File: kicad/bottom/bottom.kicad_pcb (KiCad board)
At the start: 2 copper layers, 62 x 119.5 mm, 17 parts, among them J1 Conn_01x15_Socket

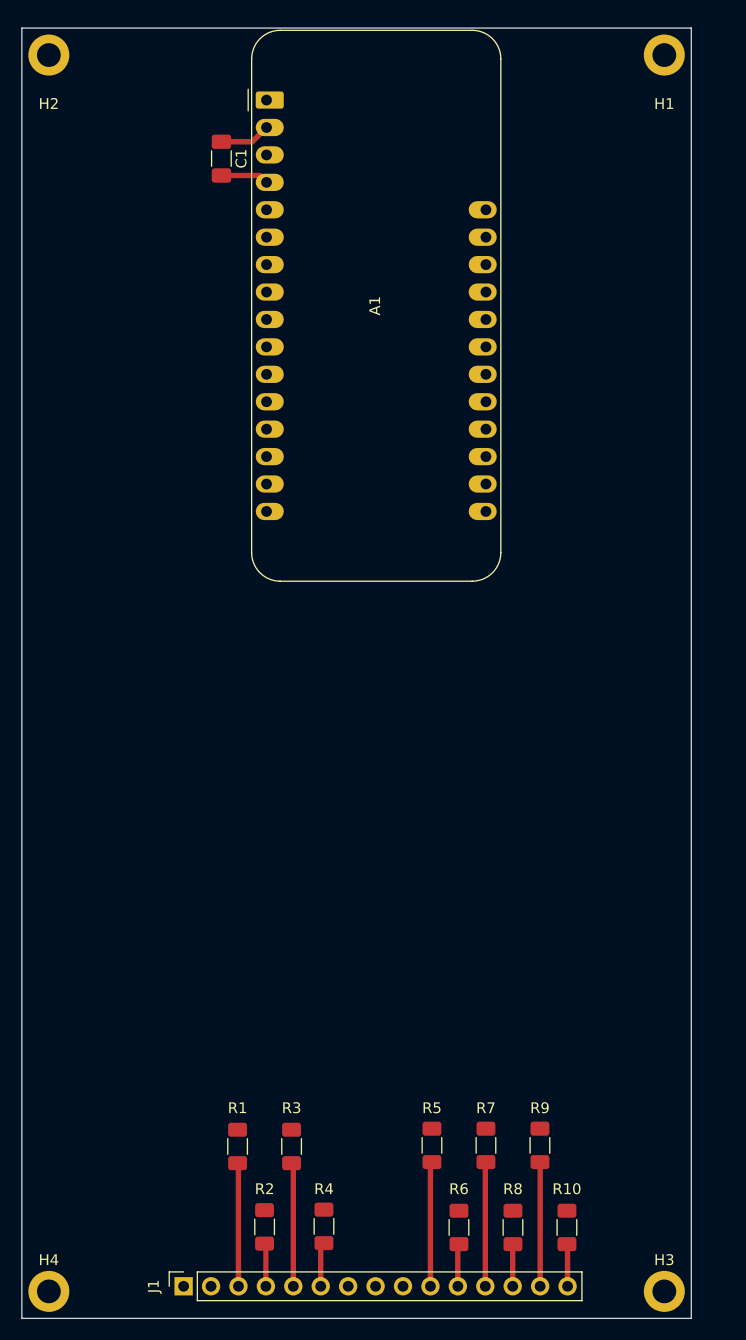
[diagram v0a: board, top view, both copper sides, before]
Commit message: delete duplicate top folder, finished wiring on bottom pcb, need better wiring on top pcb
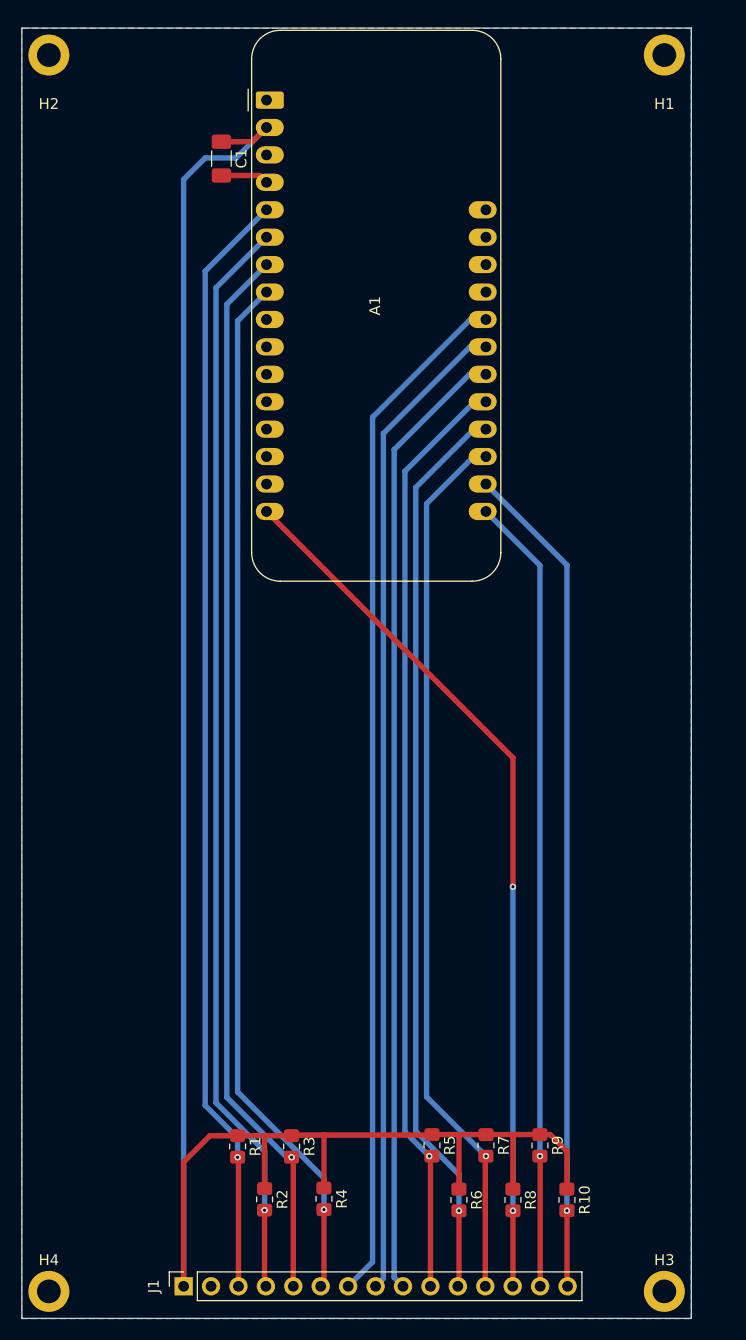
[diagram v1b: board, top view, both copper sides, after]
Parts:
- R1, R10, R2, R3, R4, R5, R6, R7, R8, R9: footprint Resistor_SMD:R_1206_3216Metric_Pad1.30x1.75mm_HandSolder -> Resistor_SMD:R_0805_2012Metric_Pad1.20x1.40mm_HandSolder
- moved R10 2.55 mm to (66.0, 125.0)
- moved R2 2.55 mm to (38.0, 125.0)
- moved R4 2.55 mm to (43.5, 124.9)
- moved R6 2.55 mm to (56.0, 125.0)
- moved R8 2.55 mm to (61.0, 125.0)
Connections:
- H1 pad 1: unconnected-(H1-Pad1) -> GND
- H2 pad 1: unconnected-(H2-Pad1) -> GND
- H3 pad 1: unconnected-(H3-Pad1) -> GND
- H4 pad 1: unconnected-(H4-Pad1) -> GND
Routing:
- net +3.3V: track 4.73 -> 188.9 mm
- net BT_SELECT: track 3.83 -> 100.8 mm, vias 0 -> 1
- net COL0: track 0.00 -> 95.7 mm
- net ENC_CLK: track 3.70 -> 96.2 mm, vias 0 -> 1
- net COL1: track 0.00 -> 92.1 mm
- net ENC_DT: track 11.3 -> 102.7 mm, vias 0 -> 1
- net COL2: track 0.00 -> 89.2 mm
- net ENC_SW: track 11.2 -> 98.2 mm, vias 0 -> 1
- net ROW2: track 3.80 -> 83.2 mm, vias 0 -> 1
- net ROW0: track 3.88 -> 81.2 mm, vias 0 -> 2
- net OLED_SCL: track 3.84 -> 77.3 mm, vias 0 -> 1
- net ROW3: track 11.4 -> 84.8 mm, vias 0 -> 1
- net ROW1: track 11.4 -> 80.3 mm, vias 0 -> 1
- net OLED_SDA: track 11.5 -> 73.3 mm, vias 0 -> 1
- added copper zone on B.Cu, net GND

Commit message: on bottom pcb moved signal connections from back copper to front, left most back copper as ground plane. aligned pins and pin sockets on top and bottom pcb, centered them.
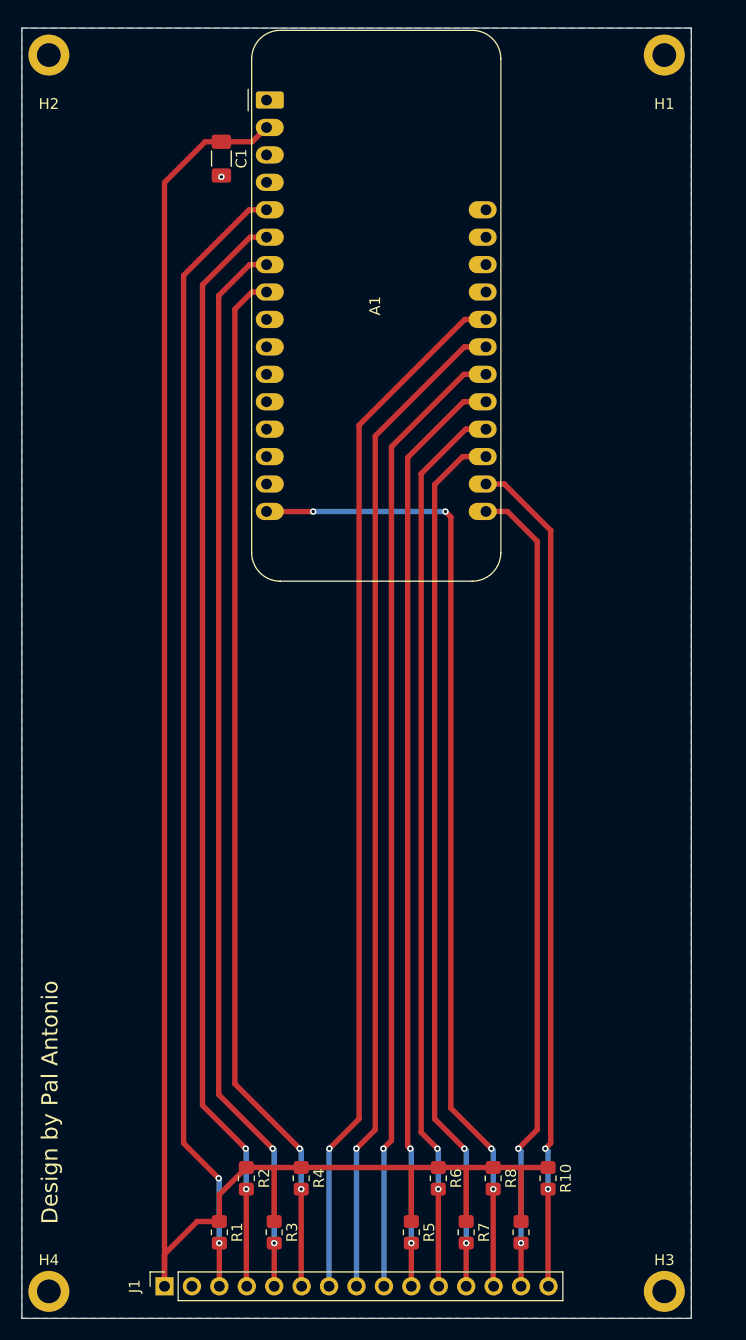
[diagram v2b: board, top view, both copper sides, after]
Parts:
- moved R5 8.27 mm to (51.6, 128.0)
- moved R7 8.26 mm to (56.7, 128.0)
- moved R9 8.24 mm to (61.8, 128.0)
- moved R1 8.13 mm to (33.8, 128.0)
- moved R3 8.11 mm to (38.9, 128.0)
- moved R4 2.84 mm to (41.4, 123.0)
- moved R6 2.77 mm to (54.1, 123.0)
- moved R8 2.71 mm to (59.2, 123.0)
- moved R10 2.66 mm to (64.2, 123.0)
- moved R2 2.58 mm to (36.3, 123.0)
- moved J1 1.77 mm to (28.7, 133.0)
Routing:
- net +3.3V: track 188.9 -> 177.2 mm
- net ROW0: track 81.2 -> 90.2 mm, vias 2 -> 4
- net GND: track 4.44 -> 0.00 mm, vias 0 -> 1
- net ENC_DT: track 102.7 -> 105.2 mm, vias 1 -> 2
- net OLED_SDA: track 73.3 -> 75.7 mm, vias 1 -> 2
- net ROW3: track 84.8 -> 86.3 mm, vias 1 -> 2
- net BT_SELECT: track 100.8 -> 102.2 mm, vias 1 -> 2
- net ENC_SW: track 98.2 -> 99.5 mm, vias 1 -> 2
- net COL1: track 92.1 -> 93.1 mm, vias 0 -> 1
- net COL0: track 95.7 -> 96.7 mm, vias 0 -> 1
- net ROW1: track 80.3 -> 81.3 mm, vias 1 -> 2
- net OLED_SCL: track 77.3 -> 78.1 mm, vias 1 -> 2
- net ROW2: track 83.2 -> 83.6 mm, vias 1 -> 2
- net ENC_CLK: track 96.2 -> 96.6 mm, vias 1 -> 2
- net COL2: track 89.2 -> 89.6 mm, vias 0 -> 1
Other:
- board text added: "Design by Pal Antonio"

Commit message: added cutout for battery jst connector on bottom pcb
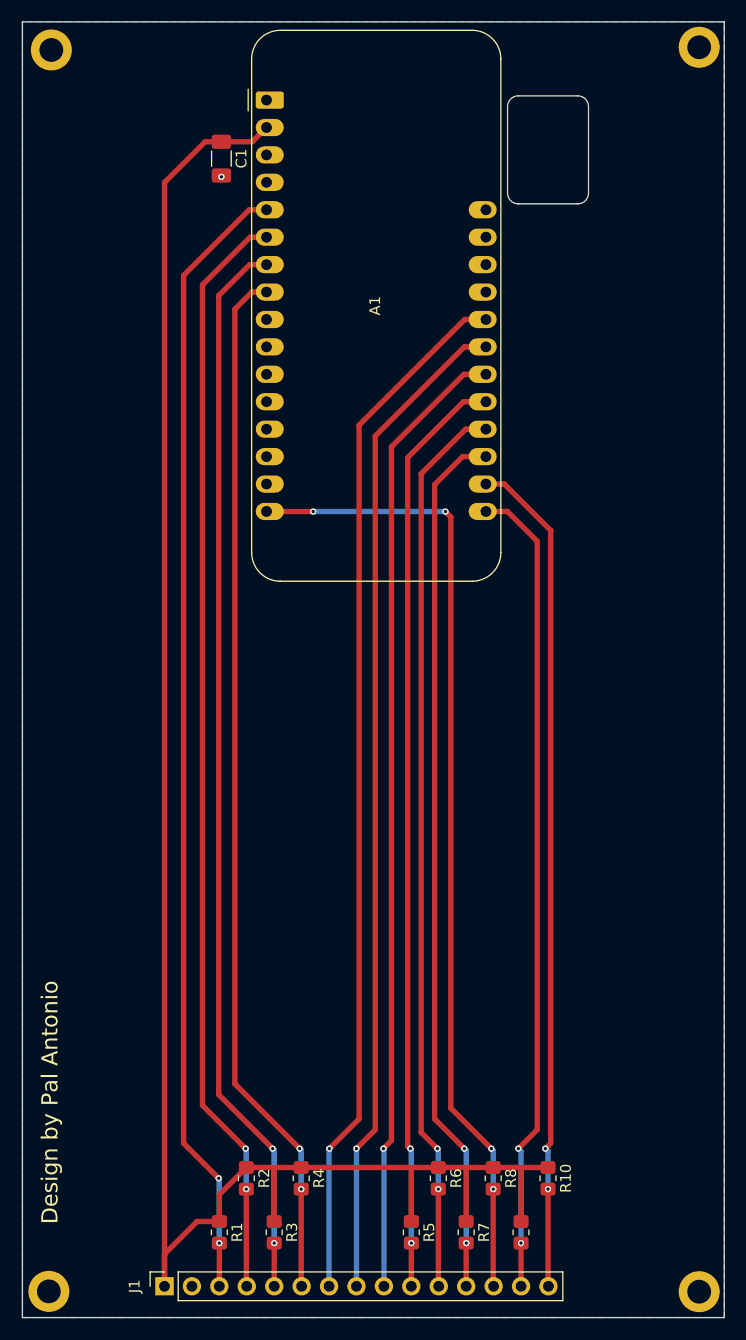
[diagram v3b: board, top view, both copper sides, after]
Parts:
- moved H2 60.2 mm to (78.2, 18.2)
- moved H1 56.8 mm to (18.2, 18.5)
- moved H3 3.23 mm to (78.2, 133.5)
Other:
- board size 62 x 119.5 mm -> 65 x 120 mm

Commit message: moved pull up res closer to pins on bottom pcb
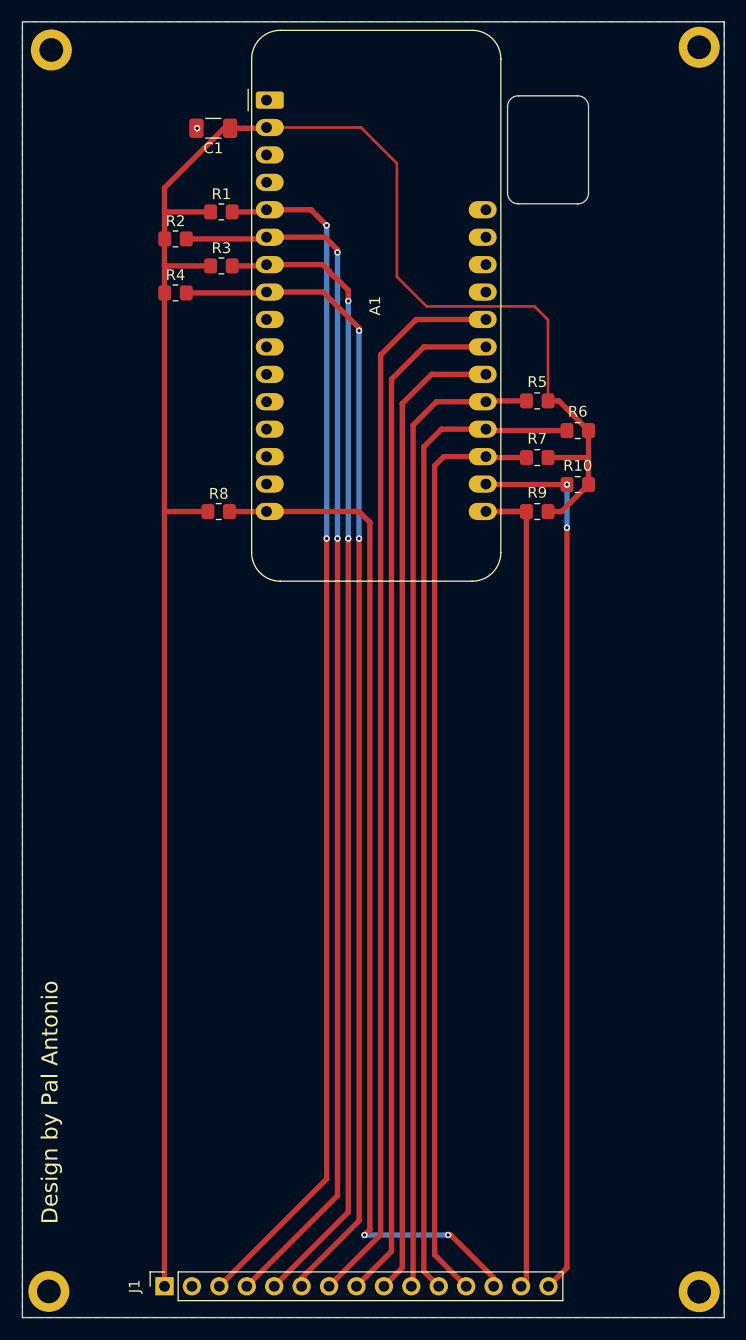
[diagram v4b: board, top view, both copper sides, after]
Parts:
- moved R1 94.5 mm to (34.0, 33.5), turned to 0 degrees
- moved R3 89.6 mm to (34.0, 38.5), turned to 0 degrees
- moved R2 87.2 mm to (29.8, 36.0), turned to 0 degrees
- moved R4 82.8 mm to (29.8, 41.0), turned to 0 degrees
- moved R5 77.9 mm to (63.2, 51.0), turned to 180 degrees
- moved R7 72.1 mm to (63.2, 56.2), turned to 180 degrees
- moved R6 70.4 mm to (67.0, 53.8), turned to 180 degrees
- moved R8 66.8 mm to (33.8, 61.2), turned to 0 degrees
- moved R9 66.8 mm to (63.2, 61.2), turned to 180 degrees
- moved R10 64.3 mm to (67.0, 58.8), turned to 180 degrees
- moved C1 2.91 mm to (33.2, 25.8), turned to 180 degrees
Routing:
- net +3.3V: track 177.2 -> 191.5 mm
- net ENC_CLK: track 96.6 -> 108.3 mm
- net BT_SELECT: track 102.2 -> 113.3 mm
- net ROW2: track 83.6 -> 92.1 mm, vias 2 -> 0
- net ENC_SW: track 99.5 -> 106.7 mm
- net ENC_DT: track 105.2 -> 111.5 mm
- net ROW1: track 81.3 -> 85.9 mm, vias 2 -> 0
- net ROW3: track 86.3 -> 90.9 mm, vias 2 -> 0
- net OLED_SCL: track 78.1 -> 82.4 mm
- net ROW0: track 90.2 -> 94.0 mm, vias 4 -> 2
- net OLED_SDA: track 75.7 -> 79.4 mm, vias 2 -> 0
- net COL0: track 96.7 -> 99.3 mm, vias 1 -> 0
- net COL1: track 93.1 -> 95.3 mm, vias 1 -> 0
- net COL2: track 89.6 -> 91.3 mm, vias 1 -> 0

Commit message: modify paths and file locations for portability, added mounting pins to encoder, changed symbol, footprint and 3d of switch to correlate to what im using
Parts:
- A1: footprint Module:Adafruit_Feather -> Bottom-Footprints:Adafruit_Feather
- C1: footprint Capacitor_SMD:C_1206_3216Metric_Pad1.33x1.80mm_HandSolder -> Bottom-Footprints:C_1206_3216Metric_Pad1.33x1.80mm_HandSolder
- H1, H2, H3, H4: footprint MountingHole:MountingHole_2.2mm_M2_DIN965_Pad -> Bottom-Footprints:MountingHole_2.2mm_M2_DIN965_Pad
- J1: footprint Connector_PinSocket_2.54mm:PinSocket_1x15_P2.54mm_Vertical -> Bottom-Footprints:PinSocket_1x15_P2.54mm_Vertical
- R1, R10, R2, R3, R4, R5, R6, R7, R8, R9: footprint Resistor_SMD:R_0805_2012Metric_Pad1.20x1.40mm_HandSolder -> Bottom-Footprints:R_0805_2012Metric_Pad1.20x1.40mm_HandSolder

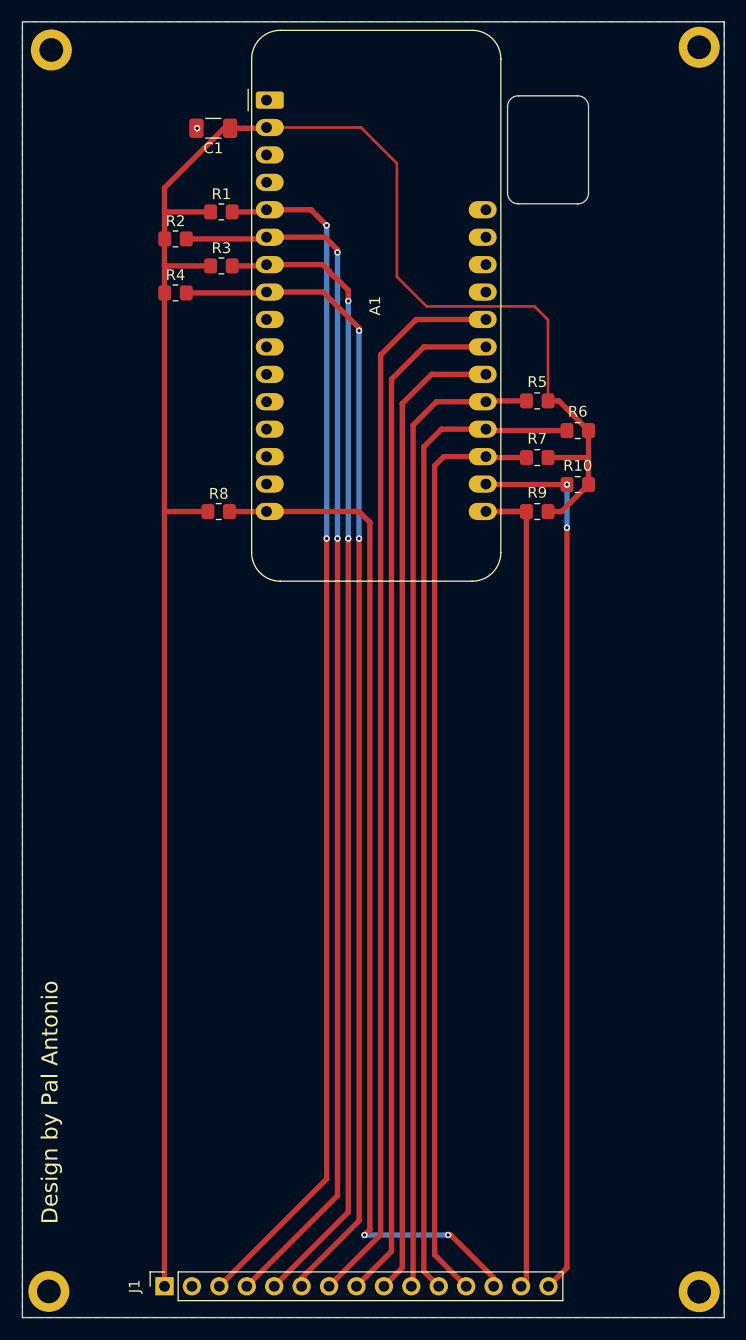
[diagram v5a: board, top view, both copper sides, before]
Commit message: finalised mounting hole and pins position, changed gpios
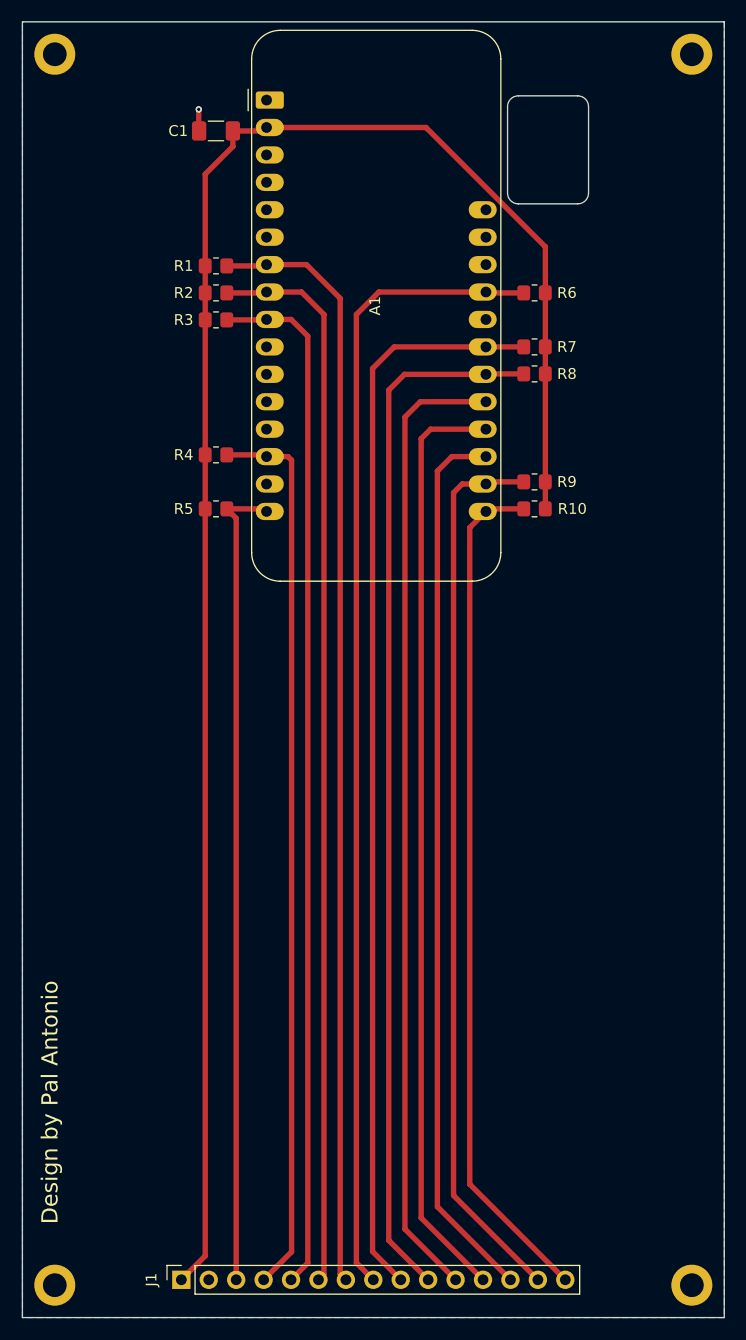
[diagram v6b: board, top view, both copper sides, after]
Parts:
- moved R8 31.9 mm to (63.0, 48.5), turned to 180 degrees
- moved R5 31.4 mm to (33.5, 61.0), turned to 0 degrees
- moved R4 15.5 mm to (33.5, 56.0)
- moved R6 13.4 mm to (63.0, 41.0)
- moved R7 10.3 mm to (63.0, 46.0)
- moved R2 6.25 mm to (33.5, 41.0)
- moved R1 5.02 mm to (33.5, 38.5)
- moved R3 5.02 mm to (33.5, 43.5)
- moved R10 4.59 mm to (63.0, 61.0)
- moved R9 2.76 mm to (63.0, 58.5)
- moved J1 1.67 mm to (30.3, 132.4)
- moved H2 0.94 mm to (77.6, 18.9)
- moved H3 0.91 mm to (77.6, 132.9)
- moved H4 0.80 mm to (18.6, 132.9)
- moved H1 0.51 mm to (18.6, 18.9)
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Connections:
- A1 pad 14: unconnected-(A1-RX-Pad14) -> BT_SELECT
- A1 pad 16: ROW0 -> ROW3
- A1 pad 19: ROW1 -> COL2
- A1 pad 20: ROW2 -> COL1
- A1 pad 21: ROW3 -> COL0
- A1 pad 22: COL2 -> ENC_SW
- A1 pad 23: COL1 -> ENC_DT
- A1 pad 24: COL0 -> unconnected-(A1-D12-Pad24)
- A1 pad 25: unconnected-(A1-LED-Pad25) -> ENC_CLK
- A1 pad 5: ENC_DT -> unconnected-(A1-A0-Pad5)
- A1 pad 6: BT_SELECT -> unconnected-(A1-A1-Pad6)
- A1 pad 7: ENC_SW -> ROW0
- A1 pad 8: ENC_CLK -> ROW1
- A1 pad 9: unconnected-(A1-A4-Pad9) -> ROW2
- J1 pad 10: ROW3 -> ENC_SW
- J1 pad 11: ROW2 -> COL0
- J1 pad 12: ROW1 -> COL1
- J1 pad 13: ROW0 -> COL2
- J1 pad 14: OLED_SDA -> OLED_SCL
- J1 pad 15: OLED_SCL -> OLED_SDA
- J1 pad 3: ENC_DT -> ROW3
- J1 pad 5: ENC_SW -> ROW2
- J1 pad 6: ENC_CLK -> ROW1
- J1 pad 7: COL0 -> ROW0
- J1 pad 8: COL1 -> ENC_CLK
- J1 pad 9: COL2 -> ENC_DT
- R1 pad 2: ENC_DT -> ROW0
- R10 pad 2: OLED_SCL -> OLED_SDA
- R2 pad 2: BT_SELECT -> ROW1
- R3 pad 2: ENC_SW -> ROW2
- R4 pad 2: ENC_CLK -> BT_SELECT
- R6 pad 2: ROW2 -> ENC_CLK
- R7 pad 2: ROW1 -> ENC_DT
- R8 pad 2: ROW0 -> ENC_SW
- R9 pad 2: OLED_SDA -> OLED_SCL
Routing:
- net BT_SELECT: track 113.3 -> 83.2 mm, vias 2 -> 0
- net +3.3V: track 191.5 -> 166.3 mm
- net ROW3: track 90.9 -> 75.5 mm
- net ROW1: track 85.9 -> 99.5 mm
- net ENC_DT: track 111.5 -> 100.3 mm, vias 2 -> 0
- net ENC_SW: track 106.7 -> 97.0 mm, vias 2 -> 0
- net COL0: track 99.3 -> 89.9 mm
- net ROW0: track 94.0 -> 103.0 mm, vias 2 -> 0
- net COL1: track 95.3 -> 86.6 mm
- net COL2: track 91.3 -> 82.8 mm
- net ROW2: track 92.1 -> 96.2 mm
- net GND: track 0.00 -> 2.02 mm
- net ENC_CLK: track 108.3 -> 106.4 mm, vias 2 -> 0
- net OLED_SCL: track 82.4 -> 83.0 mm, vias 2 -> 0
